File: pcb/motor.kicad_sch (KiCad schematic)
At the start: 13 parts, among them J1 A3144, M1 Stepper_Motor_bipolar, U2 TMC2209-LA

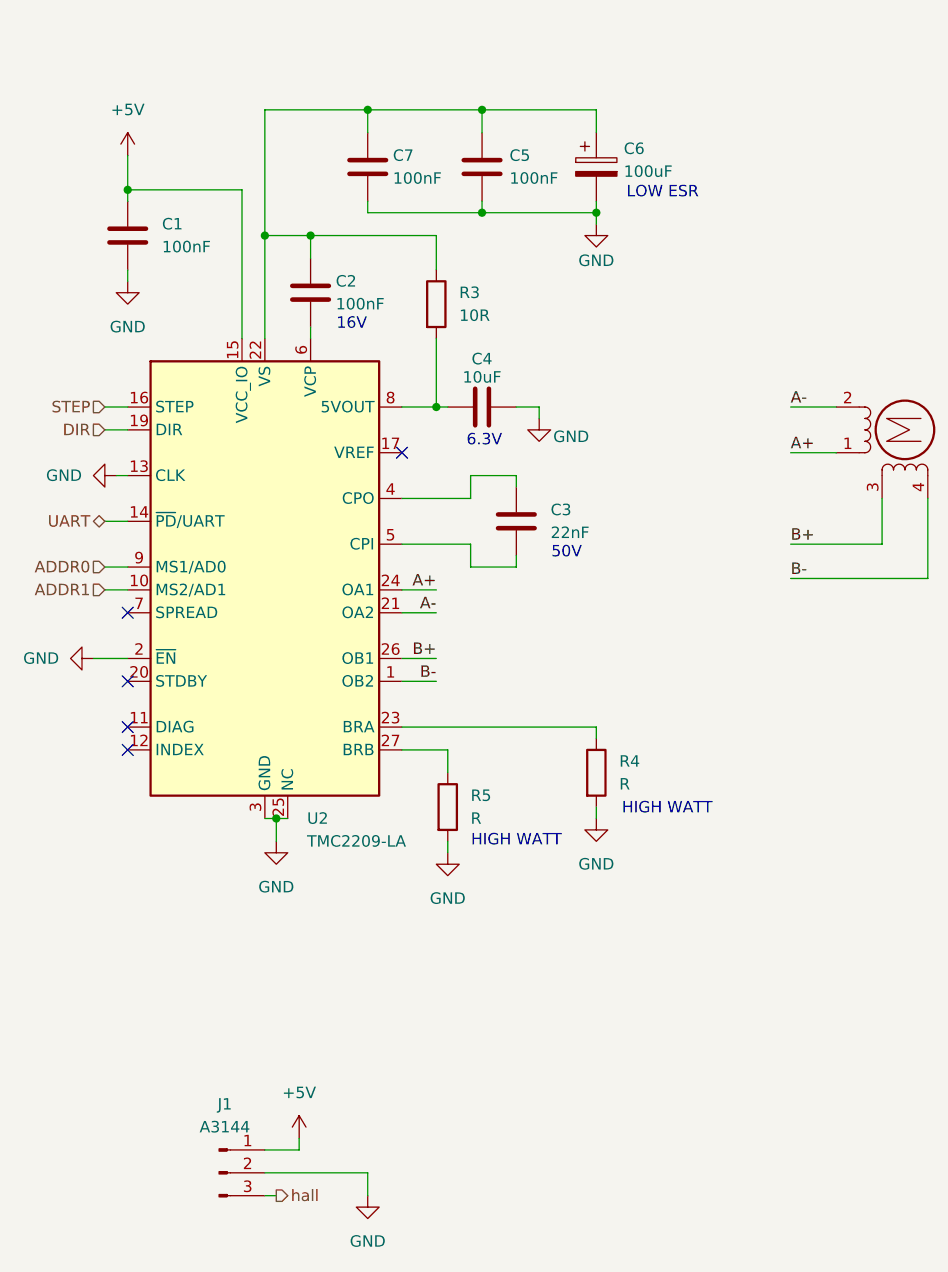
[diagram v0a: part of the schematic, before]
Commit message: feat(pcb/leds): add seconds indicator light bar and misc rgb indicator
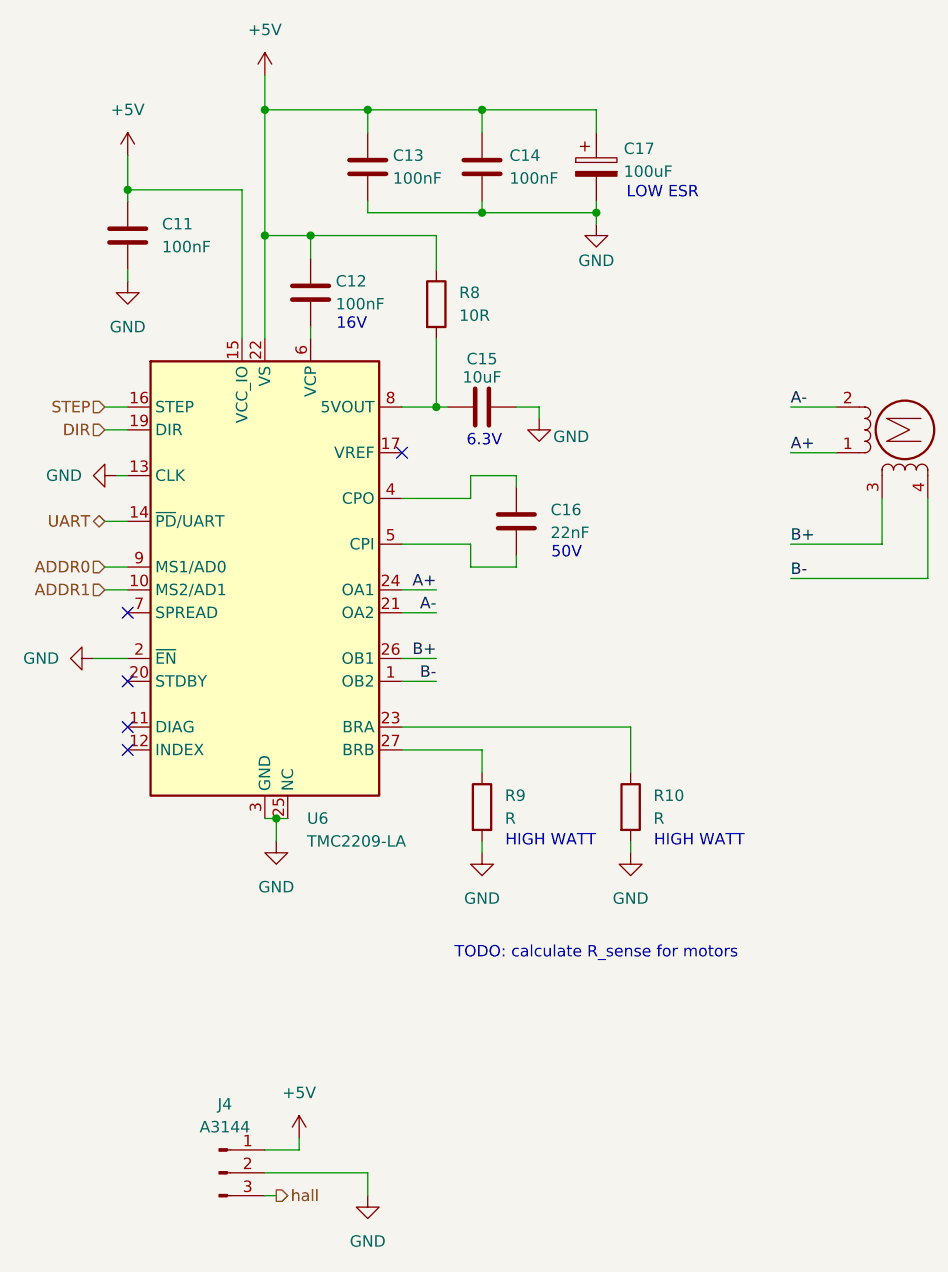
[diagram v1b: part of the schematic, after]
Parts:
- renumbered C1 to C11, C2 to C12, C7 to C13, C5 to C14, C4 to C15, C3 to C16, C6 to C17, J1 to J4, R4 to R10, R3 to R8, R5 to R9, U2 to U6
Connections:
- net +5V: now also C12.1, C13.1, C14.1, C17.1, R8.1, U6.22 (VS), U6.28 (VS)
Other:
- note added: "TODO: calculate R_sense for motors"
- moved on the sheet: R10, R9

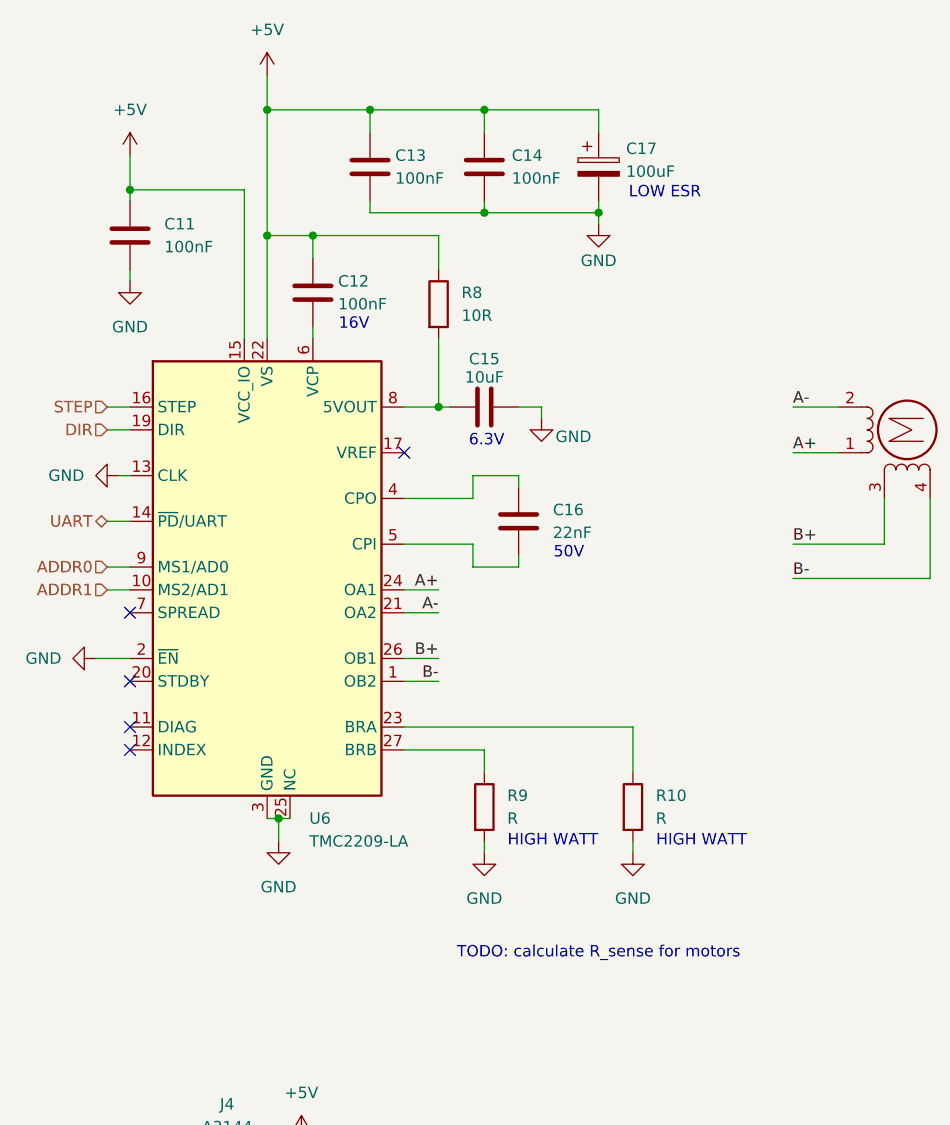
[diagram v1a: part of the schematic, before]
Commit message: feat(pcb): remove levelshifters, change to 3v3 vcc_io on tmc2209s, add rgb led to led driver, add R_ext value for led driver, add R_sense value for tmc2209s, add seperate dir signals for each tmc2209
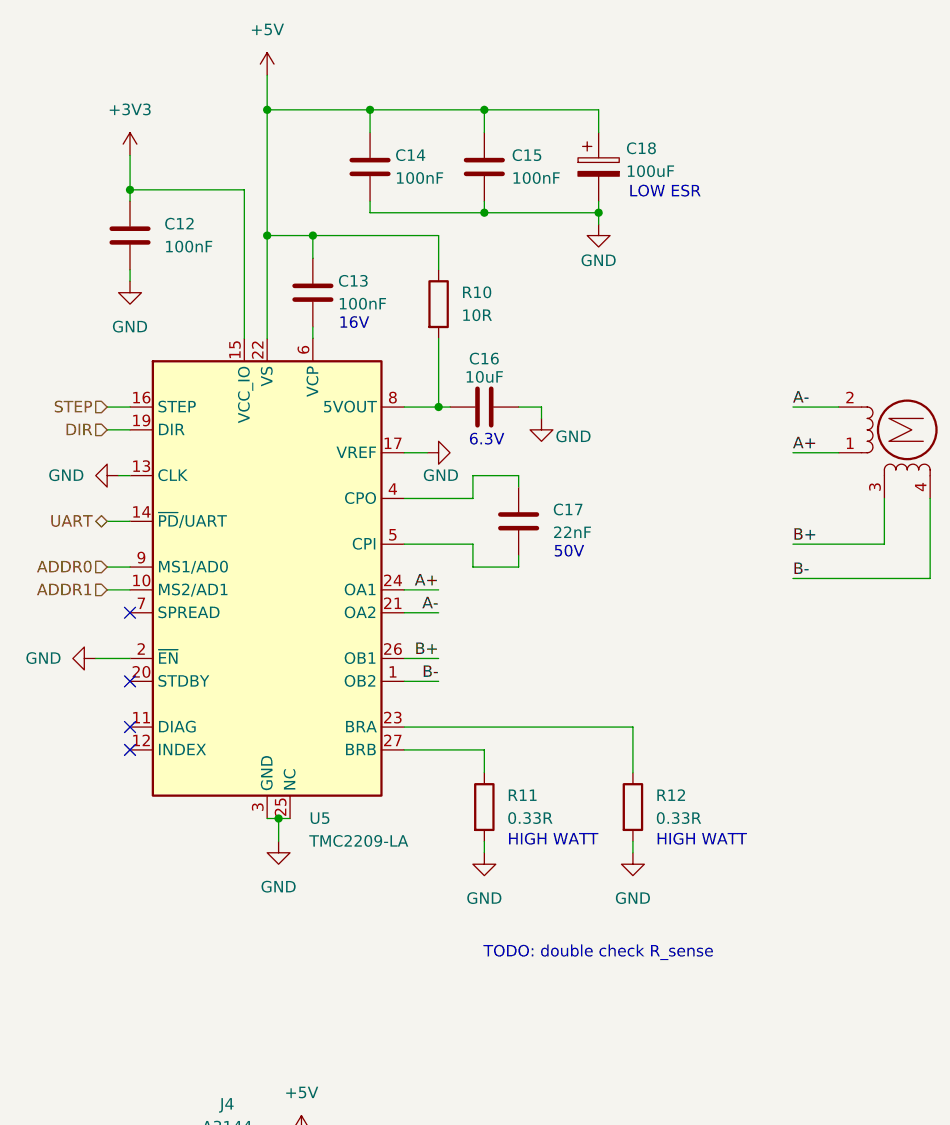
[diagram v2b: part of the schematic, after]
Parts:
- R11: renamed from R9; value R -> 0.33R
- R12: renamed from R10; value R -> 0.33R
- renumbered C11 to C12, C12 to C13, C13 to C14, C14 to C15, C15 to C16, C16 to C17, C17 to C18, R8 to R10, U6 to U5
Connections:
- net +5V: no longer C12.1, U5.15 (VCC_IO)
- net GND: now also U5.17 (VREF)
- new net +3V3: C12.1, U5.15 (VCC_IO)
- no-connect marks 5 -> 4
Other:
- note added: "TODO: double check R_sense"
- note removed: "TODO: calculate R_sense for motors"

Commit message: feat(pcb): add a central ENN connection to all motor drivers, switch LDO to one with higher input voltage tolerances and add PTC fuse
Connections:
- net GND: no longer U5.2 (~{EN})
- new net ENN: U5.2 (~{EN})

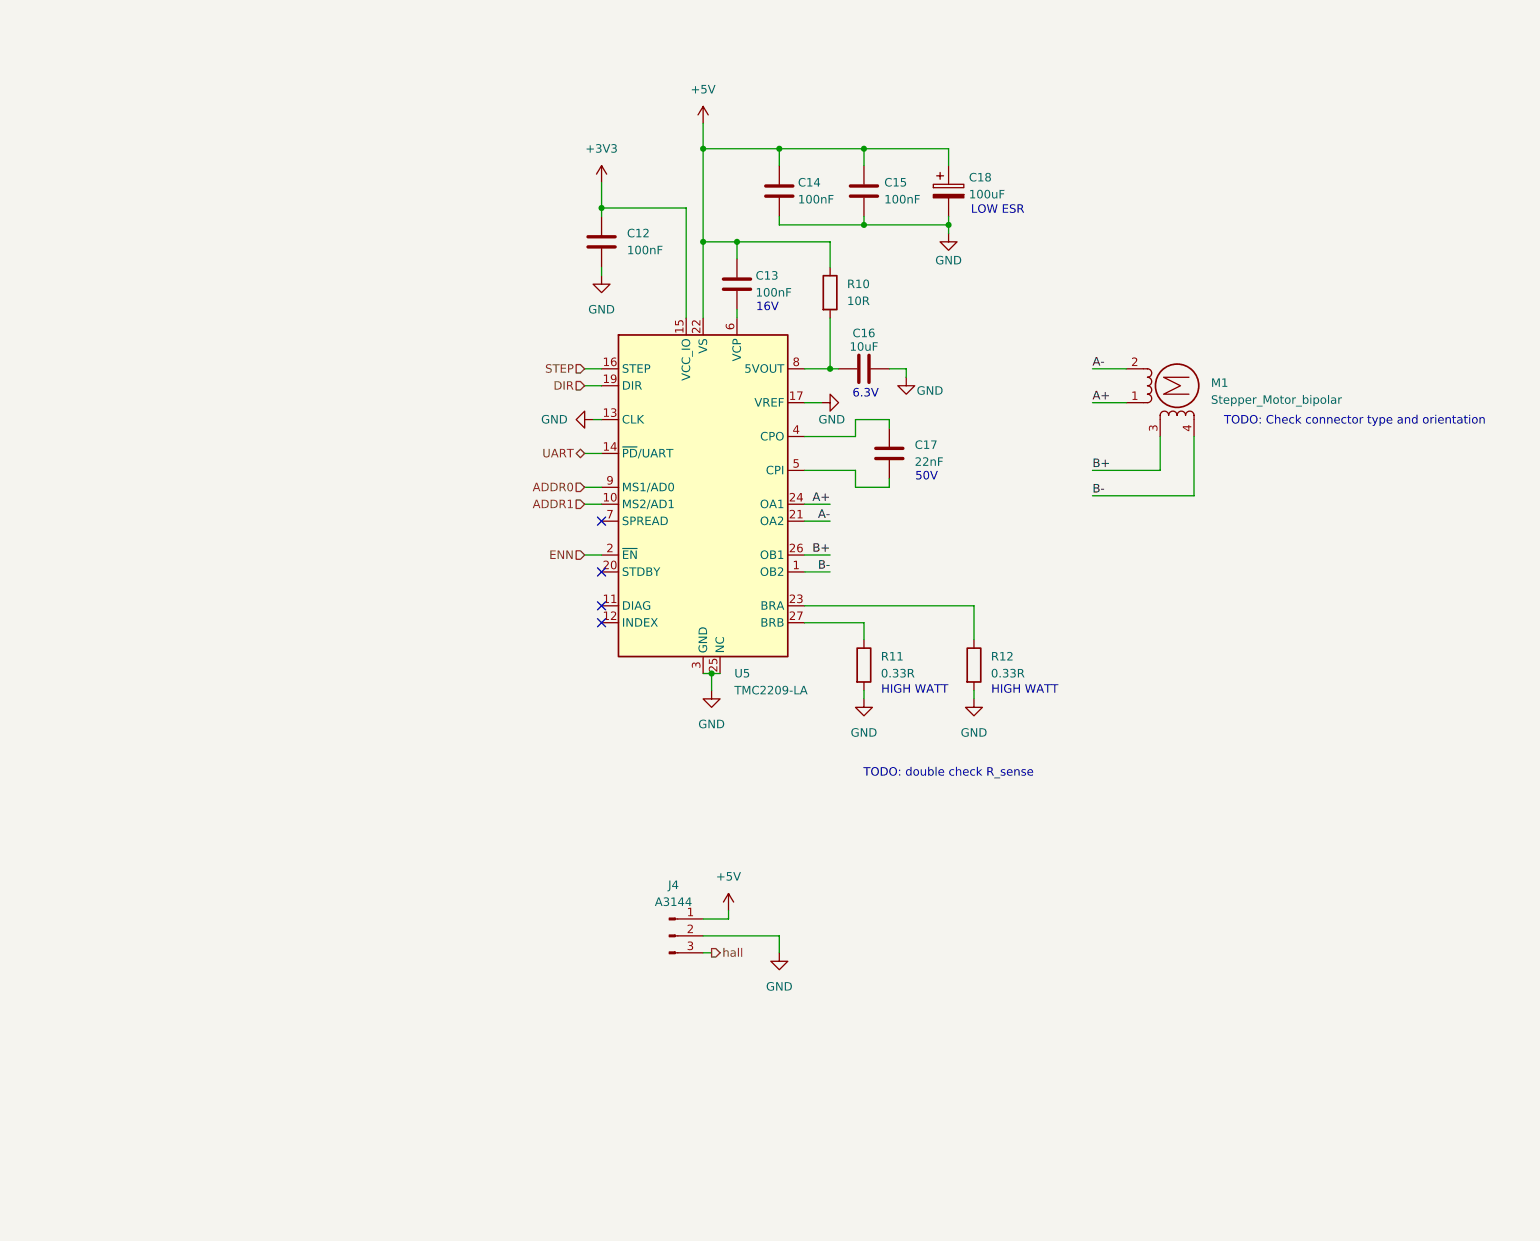
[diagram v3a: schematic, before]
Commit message: feat(pcb): source all parts, switch to straight tht usb to mount on back and add series resistor LED driver to prevent over voltage
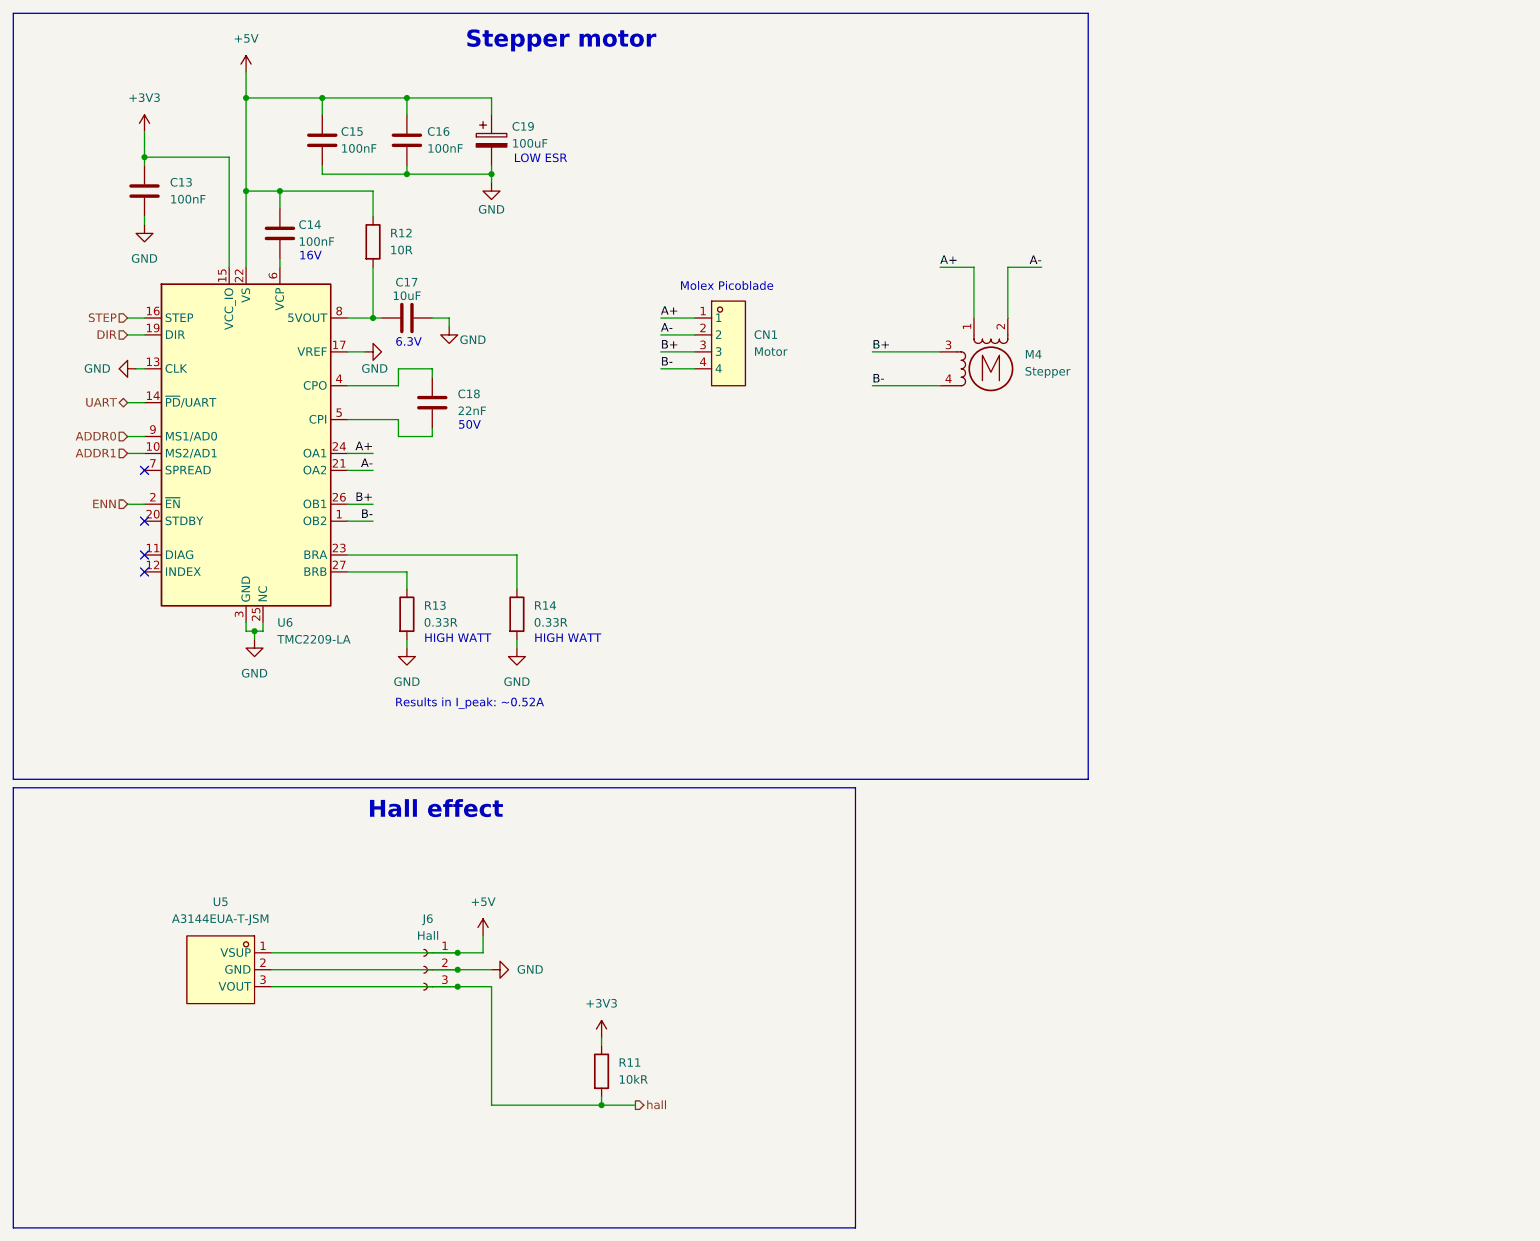
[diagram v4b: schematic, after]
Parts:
- removed J4: A3144, Connector_PinHeader_2.54mm:PinHeader_1x03_P2.54mm_Vertical, symbol Connector:Conn_01x03_Pin
- removed M1: Stepper_Motor_bipolar, lcsc:CONN-TH_530470410, symbol Motor:Stepper_Motor_bipolar
- added CN1: Motor, lcsc:CONN-TH_530470410, symbol lcsc:530470410
- added J6: Hall, Connector_PinSocket_2.54mm:PinSocket_1x03_P2.54mm_Vertical, symbol Connector:Conn_01x03_Socket
- added M4: Stepper, lcsc:CONN-TH_530470410, symbol Motor:Stepper_Motor_bipolar
- added R11: 10kR, Resistor_SMD:R_0603_1608Metric, symbol Device:R
- added U5: A3144EUA-T-JSM, lcsc:TO-92S-3_L4.1-W1.7-P1.27-L, symbol lcsc:A3144EUA-T-JSM
- C13: renamed from C12; footprint (none) -> Capacitor_SMD:C_0603_1608Metric; LCSC Part (none) -> C14663
- C14: renamed from C13; footprint (none) -> Capacitor_SMD:C_0603_1608Metric; LCSC Part (none) -> C14663
- C15: renamed from C14; footprint (none) -> Capacitor_SMD:C_0603_1608Metric; LCSC Part (none) -> C14663
- C16: renamed from C15; footprint (none) -> Capacitor_SMD:C_0603_1608Metric; LCSC Part (none) -> C14663
- C17: renamed from C16; footprint (none) -> Capacitor_SMD:C_0805_2012Metric; LCSC Part (none) -> C15850
- C18: renamed from C17; footprint (none) -> Capacitor_SMD:C_0603_1608Metric; LCSC Part (none) -> C21122
- C19: renamed from C18; footprint (none) -> lcsc:CAP-SMD_BD6.3-L6.6-W6.6-FD; LCSC Part (none) -> C320569
- R12: renamed from R10; footprint (none) -> Resistor_SMD:R_0805_2012Metric; LCSC Part (none) -> C17415
- R13: renamed from R11; footprint (none) -> Resistor_SMD:R_1206_3216Metric; LCSC Part (none) -> C2907351
- R14: renamed from R12; footprint (none) -> Resistor_SMD:R_1206_3216Metric; LCSC Part (none) -> C2907351
- renumbered U5 to U6
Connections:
- net +3V3: now also R11.1
- net +5V: now also J6.1 (Pin_1), U5.1 (VSUP)
- net A+: now also CN1.1, M4.1
- net A-: now also CN1.2, M4.2 (-)
- net B+: now also CN1.3, M4.3
- net B-: now also CN1.4, M4.4
- net GND: now also J6.2 (Pin_2), U5.2 (GND)
- net hall: now also J6.3 (Pin_3), R11.2, U5.3 (VOUT)
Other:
- note added: "Hall effect"
- note added: "Molex Picoblade"
- note added: "Results in I_peak: ~0.52A"
- note added: "Stepper motor"
- note removed: "TODO: Check connector type and orientation"
- note removed: "TODO: double check R_sense"
- moved on the sheet: C13, C14, C15, C16, C17, C18, C19, R12, R13, R14, U6

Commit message: feat(pcb): layout and route LED section
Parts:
- renumbered M4 to M1, R11 to R15

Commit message: feat(pcb): layout motor drivers and route internally
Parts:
- J6: footprint Connector_PinSocket_2.54mm:PinSocket_1x03_P2.54mm_Vertical -> Connector_JST:JST_XH_B3B-XH-AM_1x03_P2.50mm_Vertical
